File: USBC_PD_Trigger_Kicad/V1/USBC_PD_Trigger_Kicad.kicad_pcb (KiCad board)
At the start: 2 copper layers, 44.2 x 46.5 mm, 24 parts, among them J1 USB_C_Receptacle_PowerOnly_6P, J2 Screw_Terminal_01x03, SW1 SW_Push, U1 FUSB302BMPX, U2 ProMicro

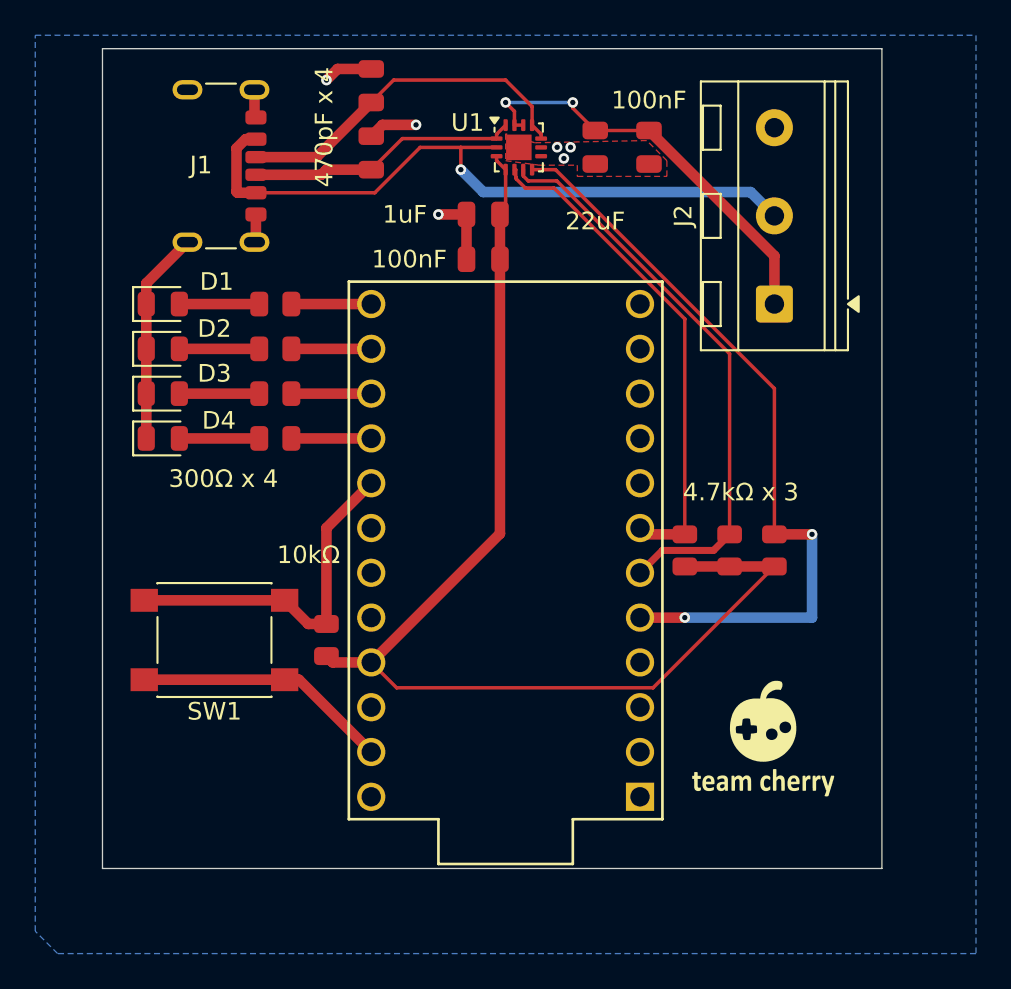
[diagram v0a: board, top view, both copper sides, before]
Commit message: Added V2 of trigger board w efuse and smaller mc
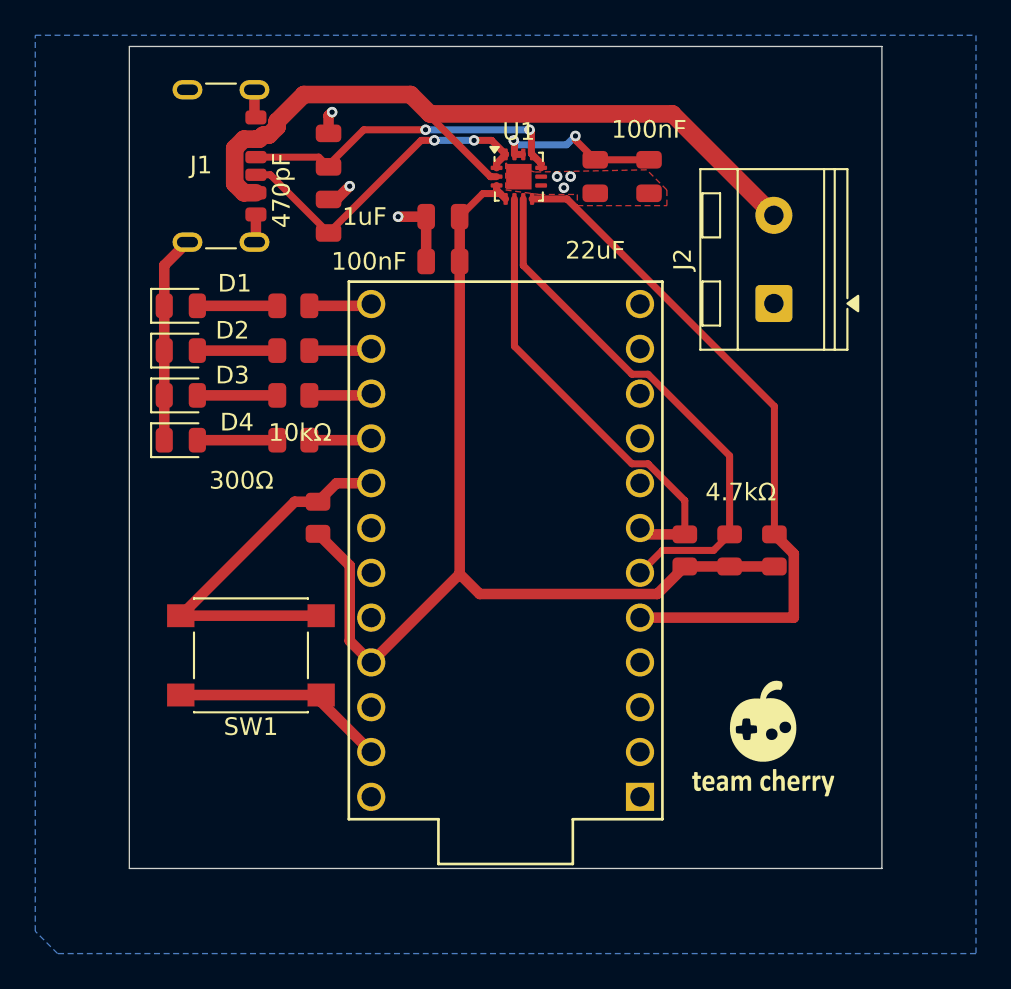
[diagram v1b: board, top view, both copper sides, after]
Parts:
- C6: value 470pF x 4 -> 470pF
- J2: value Screw_Terminal_01x03 -> Screw_Terminal_01x02; footprint TerminalBlock_RND:TerminalBlock_RND_205-00046_1x03_P5.00mm_Horizontal -> TerminalBlock_RND:TerminalBlock_RND_205-00045_1x02_P5.00mm_Horizontal
- R4: value 300Ω x 4 -> 300Ω
- Rpu_SCL1: value 4.7kΩ x 3 -> 4.7kΩ
- moved R5 6.95 mm to (55.4, 93.4)
- moved C7 4.38 mm to (56.0, 72.5)
- moved C6 4.33 mm to (56.0, 76.3)
- moved C5 2.29 mm to (62.5, 78.9)
- moved C4 2.29 mm to (62.5, 76.3)
- moved SW1 2.25 mm to (51.6, 101.2)
- moved U1 1.66 mm to (66.8, 74.1)
- moved C1 1.66 mm to (74.2, 74.0)
- moved C3 1.66 mm to (71.1, 74.0)
- moved D2 1.02 mm to (47.6, 83.9)
- moved R2 1.02 mm to (54.0, 83.9)
- moved D1 1.02 mm to (47.6, 81.4)
- moved D3 1.02 mm to (47.6, 86.5)
- moved D4 1.02 mm to (47.6, 89.0)
- moved R1 1.02 mm to (54.0, 81.4)
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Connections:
- J2 pad 1: VCONN -> GND
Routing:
- net VCONN: track 23.8 -> 9.95 mm
- net VDD: track 66.1 -> 58.7 mm
- net GND: track 39.9 -> 34.6 mm
- net /SDA: track 43.8 -> 39.8 mm, vias 2 -> 0
- net /VBUS: track 39.7 -> 43.6 mm, vias 1 -> 0
- net /CC2: track 15.5 -> 19.0 mm, vias 0 -> 2
- net /INT_N: track 28.4 -> 26.2 mm
- net /SCL: track 32.5 -> 30.4 mm
- net /IO5: track 19.9 -> 21.9 mm
- net /CC1: track 20.1 -> 19.1 mm, vias 0 -> 2
- net /IO4: track 4.53 -> 3.55 mm
- net /IO3: track 4.53 -> 3.55 mm
- net /IO1: track 4.53 -> 3.55 mm
- net /IO2: track 4.53 -> 3.55 mm
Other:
- board size 44.2 x 46.5 mm -> 42.7 x 46.6 mm
